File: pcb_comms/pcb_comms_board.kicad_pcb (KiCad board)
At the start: 2 copper layers, 90 x 90.2 mm, 106 parts, among them IC1 CP2102N-A02-GQFN28, IC2 TPS2553QDBVRQ1, IC3 TPS2553QDBVRQ1, IC4 BGS12WN6E6329XTSA1, J1 Conn_01x06_Pin, J2 Conn_02x20_Counter_Clockwise, J3 Conn_01x04, J4 SMA_CONN, J7 USB-B-Micro, U1 MAX-M10S-00B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

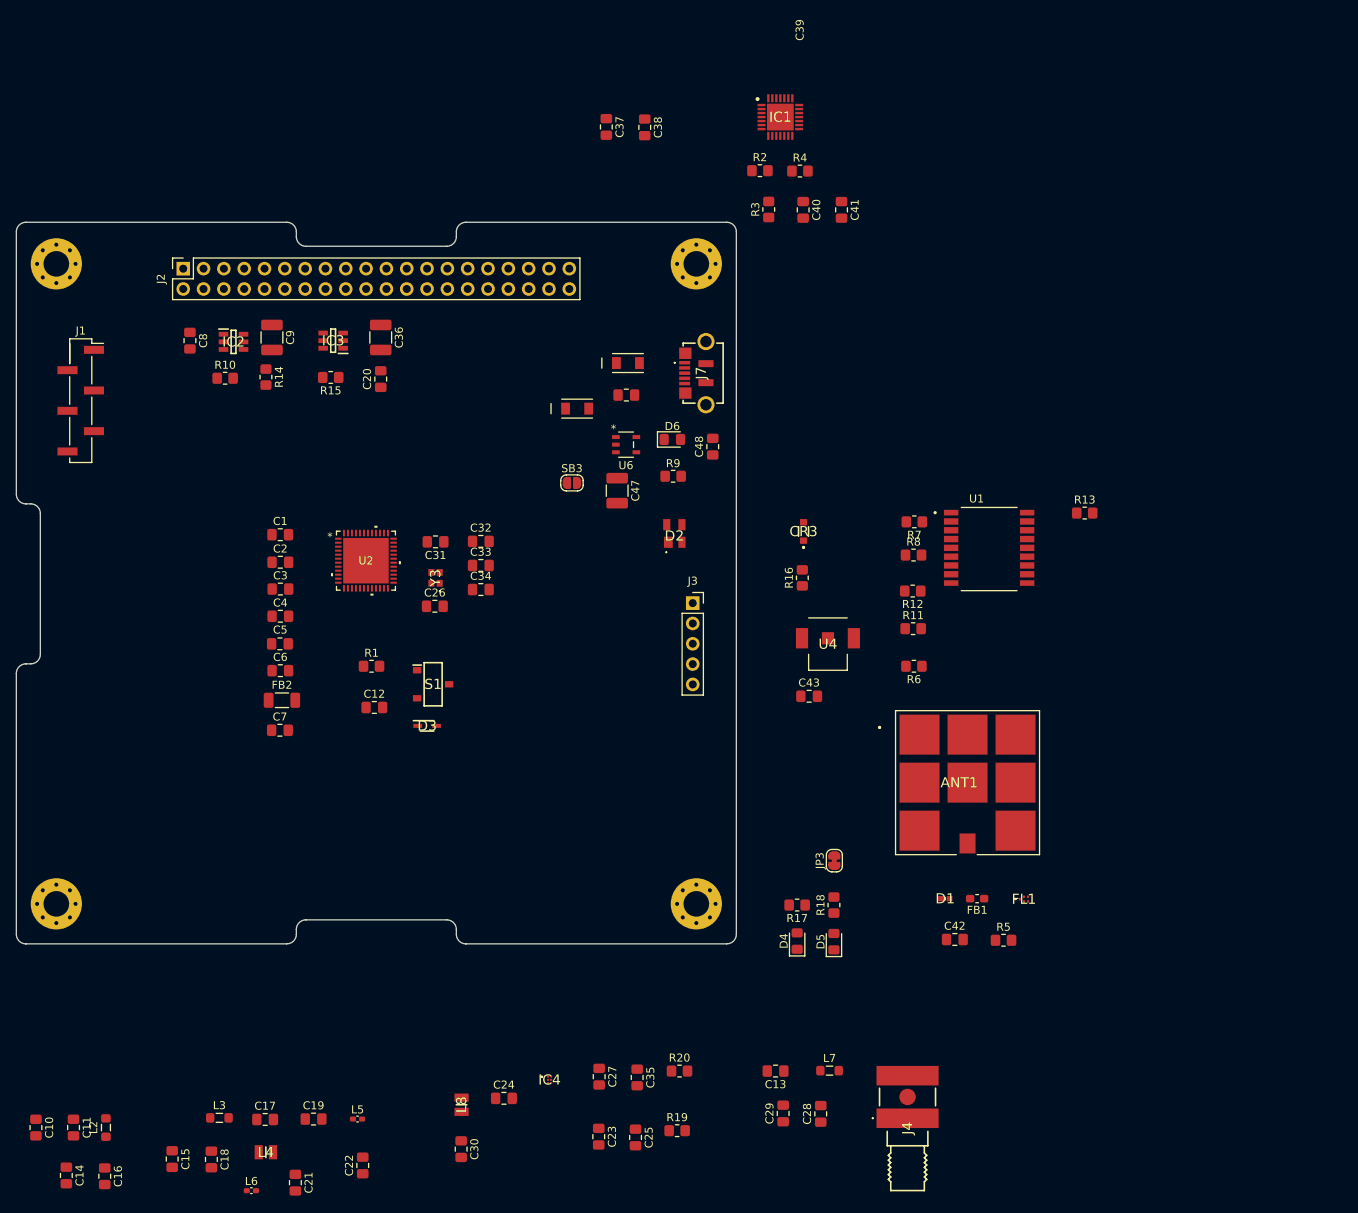
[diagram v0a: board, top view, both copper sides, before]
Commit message: Add DRA818
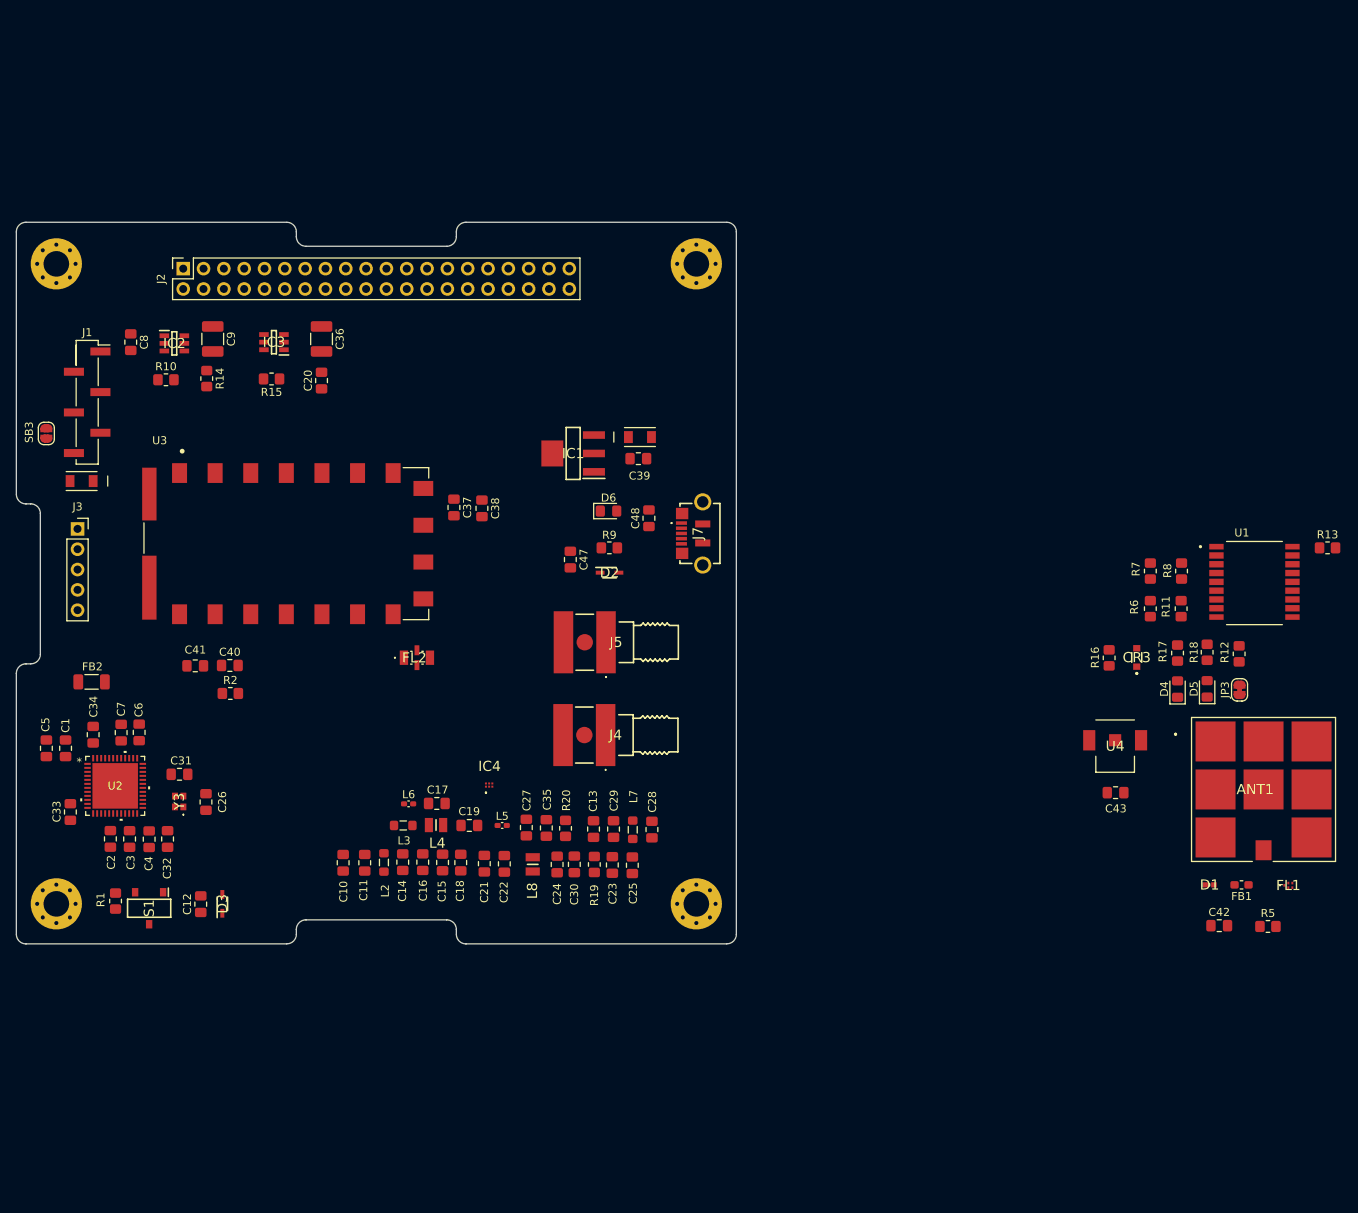
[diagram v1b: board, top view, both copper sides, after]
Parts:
- removed R3: 47.5K, Resistor_SMD:R_0805_2012Metric_Pad1.20x1.40mm_HandSolder
- removed R4: 1K, Resistor_SMD:R_0805_2012Metric_Pad1.20x1.40mm_HandSolder
- removed U6: ADP122AUJZ-3.3-R7, LDO_ADP122AUJZ_3_3_R7:UJ_5_ADI
- added FL2: LFCN-160+, RF_FILTER_LFCN-160+:RF_FILTER_LFCN-160+, F.Cu at (151.3, 100.6)
- added J5: SMA_CONN, SMA_ANTENNA_CONSMA002-SMD-G:SMA_ANTENNA_CONSMA002-SMD-G, F.Cu at (176.3, 98.7)
- added U3: DRA818V, DRA818V:DORJI_DRA818V, F.Cu at (134.9, 86.3)
- C37: value 4.7uF -> 0.1uF
- C40: value 1uF -> 0.1uF
- C41: value 0.1uF -> 4.7uF
- C47: value 100uF -> 1uF; footprint Capacitor_SMD:C_1210_3225Metric_Pad1.33x2.70mm_HandSolder -> Capacitor_SMD:C_0805_2012Metric_Pad1.18x1.45mm_HandSolder
- C48: value 10uF -> 4.7uF
- D2: value SP0503BAHTG -> AQ3530-01FTG; footprint ESD_PROTECTION_DIODE_SP0503BAHTG:ESD_PROTECTION_DIODE_SP0503BAHTG -> ESD_PROTECTION_DIODE_AQ3530-01FTG:ESD_PROTECTION_DIODE_AQ3530-01FTG
- IC1: value CP2102N-A02-GQFN28 -> LDL1117S33R; footprint USB_TO_UART_BRIDGE_CP2102N:USB_TO_UART_BRIDGE_CP2102N-A02-GQFN28 -> LDO_LDL1117S33R:LDO_LDL1117S33R
- R2: value 22.1K -> 270R
- moved C41 98.9 mm to (123.6, 101.6), turned to 180 degrees
- moved R2 93.0 mm to (128.0, 105.0)
- moved C40 91.5 mm to (127.9, 101.5), turned to 0 degrees
- moved J3 77.5 mm to (108.8, 84.5)
- moved SB3 66.0 mm to (105.0, 72.5), turned to -90 degrees
- moved CR2 62.6 mm to (109.4, 78.5), turned to 180 degrees
- moved J4 61.3 mm to (176.3, 110.2), turned to 180 degrees
- moved C33 59.9 mm to (108.0, 119.9), turned to -90 degrees
- moved C14 57.5 mm to (149.5, 126.1)
- moved D4 57.0 mm to (246.3, 104.5)
- moved R17 57.0 mm to (246.3, 100.0), turned to -90 degrees
- moved D5 56.3 mm to (250.1, 104.5)
- moved R18 56.3 mm to (250.1, 99.9)
- moved C16 55.9 mm to (152.0, 126.1)
- moved JP3 55.0 mm to (254.1, 104.6)
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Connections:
- C37 pad 1: +3.3V -> VBAT
- C38 pad 1: +3.3V -> VBAT
- C40 pad 1: Net-(IC1-VBUS) -> STM32_TO_DRA_AUDIO
- C41 pad 1: Net-(IC1-VBUS) -> STM32_TO_DRA_AUDIO
- C41 pad 2: GND -> /RF/MIC_IN
- D2 pad 1: GND -> /IO_CONN/VBUS
- D2 pad 2: /IO_CONN/VBUS -> GND
- IC1 pad 1: unconnected-(IC1-DCD-Pad1) -> GND
- IC1 pad 3: GND -> +5V
- IC1 pad 4: /IO_CONN/USB_D+ -> +3.3V
- J7 pad 2: /IO_CONN/USB_D- -> unconnected-(J7-D--Pad2)
- J7 pad 3: /IO_CONN/USB_D+ -> unconnected-(J7-D+-Pad3)
- R2 pad 1: /IO_CONN/VBUS -> STM32_TO_DRA_AUDIO
- R2 pad 2: Net-(IC1-VBUS) -> GND
- U2 pad 38: unconnected-(U2-PC13-Pad38) -> DRA_ENA
- U2 pad 39: unconnected-(U2-PC14-OSC32_IN-Pad39) -> DRA_PTT
- U2 pad 4: USB_RX_TO_STM32 -> DRA_RX_UART1
- U2 pad 40: unconnected-(U2-PC15-OSC32_OUT-Pad40) -> STM32_TO_DRA_AUDIO
- U2 pad 5: USB_TX_TO_STM32 -> DRA_TX_UART1

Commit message: remove gps
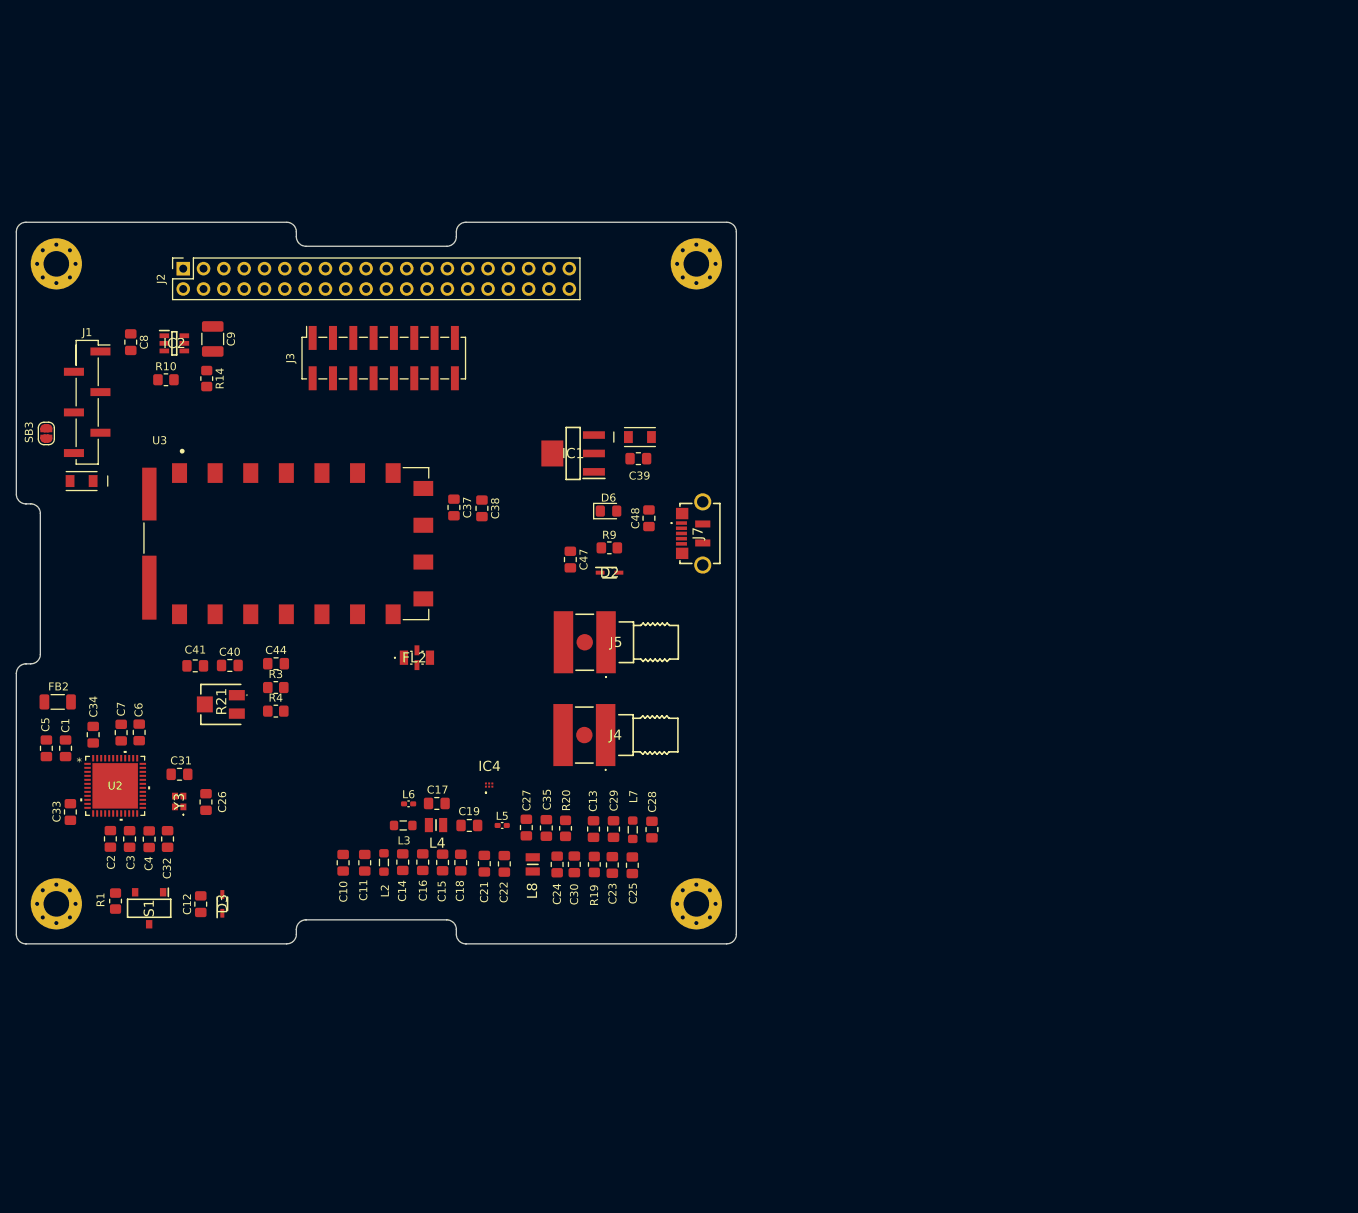
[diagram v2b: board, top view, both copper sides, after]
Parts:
- removed ANT1: SGGP.18.4.A.08, GPS_Antenna_SGGP.18.4.A.08:GPS_Antenna_SGGP.18.4.A.08
- removed C20: 10uF, Capacitor_SMD:C_0805_2012Metric_Pad1.18x1.45mm_HandSolder
- removed C36: 150uF, Capacitor_SMD:C_1210_3225Metric_Pad1.33x2.70mm_HandSolder
- removed C42: 47pF, Capacitor_SMD:C_0805_2012Metric_Pad1.18x1.45mm_HandSolder
- removed C43: 1uF, Capacitor_SMD:C_0805_2012Metric_Pad1.18x1.45mm_HandSolder
- removed CR3: CUS10S30,H3F, SCHOTTKY_DIODE_CUS10S30,H3F:SCHOTTKY_DIODE_CUS10S30,H3F
- removed D1: PESD0402-140, ESD_PROTECTION_DIODE_PESD0402-140:ESD_PROTECTION_DIODE_PESD0402-140
- removed D4: RED, LED_SMD:LED_0805_2012Metric_Pad1.15x1.40mm_HandSolder
- removed D5: YELLOW, LED_SMD:LED_0805_2012Metric_Pad1.15x1.40mm_HandSolder
- removed FB1: 3R, Inductor_SMD:L_0603_1608Metric_Pad1.05x0.95mm_HandSolder
- removed FL1: B39162B4348P810, GPS_SAW_FILTER:B39162B4348P810
- removed IC3: TPS2553QDBVRQ1, OCP_TPS2553QDBVRQ1:SOT95P280X145-6N
- removed JP3: PWR, Jumper:SolderJumper-2_P1.3mm_Bridged_RoundedPad1.0x1.5mm
- removed R11, R12, R13, R6, R7, R8: 33R, Resistor_SMD:R_0805_2012Metric_Pad1.20x1.40mm_HandSolder
- removed R15: 10K, Resistor_SMD:R_0805_2012Metric_Pad1.20x1.40mm_HandSolder
- removed R16: 3.3K, Resistor_SMD:R_0805_2012Metric_Pad1.20x1.40mm_HandSolder
- removed R17, R18: 1K, Resistor_SMD:R_0805_2012Metric_Pad1.20x1.40mm_HandSolder
- removed R2: 270R, Resistor_SMD:R_0805_2012Metric_Pad1.20x1.40mm_HandSolder
- removed R5: 330R, Resistor_SMD:R_0805_2012Metric_Pad1.20x1.40mm_HandSolder
- removed U1: MAX-M10S-00B, GPS_MAX_M10S:XCVR_MAX-M10S-00B
- removed U4: Coin cell, GPS_BATTERY_HOLDER_2994:GPS_BATTERY_HOLDER_2994
- added C44: 1uF, Capacitor_SMD:C_0805_2012Metric_Pad1.18x1.45mm_HandSolder, F.Cu at (133.7, 101.3)
- added R21: 3314J-1-103E, TRIMPOT_10K_3314J-1-103E:TRIMPOT_10K_3314J-1-103E, F.Cu at (126.8, 106.4)
- added R3: 10K, Resistor_SMD:R_0805_2012Metric_Pad1.20x1.40mm_HandSolder, F.Cu at (133.6, 104.3)
- added R4: 10K, Resistor_SMD:R_0805_2012Metric_Pad1.20x1.40mm_HandSolder, F.Cu at (133.6, 107.3)
- C38: value 0.1uF -> 4.7uF
- J3: value Conn_01x04 -> Conn_02x08_Counter_Clockwise; footprint Connector_PinSocket_2.54mm:PinSocket_1x05_P2.54mm_Vertical -> Connector_PinSocket_2.54mm:PinSocket_2x08_P2.54mm_Vertical_SMD
- moved J3 43.8 mm to (147.1, 63.1), turned to 90 degrees
- moved FB2 4.92 mm to (106.4, 106.1)
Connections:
- net Net-(C13-Pad1) renamed /RF/RFIN2
- net Net-(C17-Pad1) renamed /RF/RFO_TO_CAP
- net Net-(C17-Pad2) renamed /RF/RF_NODO1
- net Net-(C19-Pad2) renamed /RF/RF_C19_TO_L5
- net Net-(C28-Pad2) renamed /RF/SMA1
- net Net-(IC4-CTRL) renamed /RF/SWITCH_TO_CRL
- net Net-(IC4-RF1) renamed /RF/RF1
- net Net-(IC4-RF2) renamed /RF/RF2
- net Net-(IC4-RFIN) renamed /RF/RFIN
- net Net-(IC4-VDD) renamed /RF/VDD_SWITCH_RF
- C40 pad 1: STM32_TO_DRA_AUDIO -> Net-(R21-WIPER)
- C41 pad 1: STM32_TO_DRA_AUDIO -> Net-(R21-WIPER)
- J3 pad 1: SPI2_SCK -> AUX0_SDA
- J3 pad 2: SPI2_MOSI -> AUX1_SCL
- J3 pad 3: SPI2_MISO -> AUX2
- J3 pad 4: SPI2_CS -> AUX3
- J3 pad 5: (no net) -> AUX4
- J7 pad 4: GND -> unconnected-(J7-ID-Pad4)
- U2 pad 1: SPI1_SCK -> JTDO_SWO_TO_STM32
- U2 pad 10: MAX_TXO_TO_STM32 -> TX_UART2
- U2 pad 12: MAX_RESET_N_TO_STM32 -> RF_CRL_TO_STM32
- U2 pad 13: SPI2_MISO -> DRA_PTT
- U2 pad 14: SPI1_MISO -> DRA_ENA
- U2 pad 15: SPI2_CS -> AUX8
- U2 pad 16: SPI2_SCK -> AUX7
- U2 pad 17: RF_CRL_TO_STM32 -> AUX6
- U2 pad 2: SPI1_CS -> SPI1_MISO
- U2 pad 30: unconnected-(U2-PB0-VDD_TCXO-Pad30) -> AUX5
- U2 pad 31: STM32_TO_OCP -> AUX4
- U2 pad 32: unconnected-(U2-PB12-Pad32) -> AUX3
- U2 pad 33: SPI2_MOSI -> STM32_DAC_TO_DRA
- U2 pad 34: OCP_NFAULT_GPS -> DRA_TO_STM32_ADC
- U2 pad 35: OCP_NFAULT -> AUX1_SCL
- U2 pad 38: DRA_ENA -> AUX10
- U2 pad 39: DRA_PTT -> OCP_NFAULT
- U2 pad 40: STM32_TO_DRA_AUDIO -> AUX2
- U2 pad 43: JTDO_SWO_TO_STM32 -> AUX0_SDA
- U2 pad 6: MAX_INT_TO_STM32 -> AUX9
- U2 pad 7: MAX_PPS_TO_STM32 -> SPI1_CS
- U2 pad 8: MAX_SAFE_N_TO_STM32 -> SPI1_SCK
- U2 pad 9: MAX_RXI_TO_STM32 -> RX_UART2
- U3 pad 3: unconnected-(U3-AF_OUT-Pad3) -> Net-(U3-AF_OUT)
